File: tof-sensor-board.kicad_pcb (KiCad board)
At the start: 2 copper layers, 22.8 x 16.8 mm, 30 parts, among them U1 STM32F302K8U6, U2 LTC2875, U3 MCP1703, U4 VL53L0X, X1 16MHz

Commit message: routing finished
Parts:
- added G***: LOGO, _logo:CVRA-logo-small, B.Cu at (59.0, 56.0)
- C7: moved to F.Cu
- moved R8 4.10 mm to (49.7, 57.0), turned to 180 degrees
- moved C11 2.64 mm to (55.6, 56.4), turned to 270 degrees
- moved C7 2.61 mm to (53.4, 53.7), turned to 180 degrees
- moved R9 1.12 mm to (47.7, 52.6), turned to 0 degrees
- moved C1 0.58 mm to (53.7, 53.3)
- moved C14 0.22 mm to (52.9, 48.0)
- moved C13 0.20 mm to (46.7, 48.2), turned to 270 degrees
- moved C2 0.20 mm to (47.7, 48.2), turned to 270 degrees
- moved U2 0.20 mm to (53.1, 56.0)
- moved R6 0.14 mm to (49.5, 54.1)
- moved R7 0.14 mm to (50.5, 54.1), turned to 90 degrees
- moved D2 0.10 mm to (49.3, 54.3)
- moved D3 0.10 mm to (50.7, 54.3)
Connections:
- MEC1 pad 1: (no net) -> GND
- MEC2 pad 1: (no net) -> GND
- U1 pad 10: (no net) -> /Proximity
- U1 pad 11: /Proximity -> /Error
- U1 pad 12: /Error -> (no net)
- U1 pad 33: (no net) -> GND
- U2 pad 9: Net-(U2-Pad9) -> GND
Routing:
- net GND: track 28.1 -> 80.9 mm, vias 1 -> 8
- net /CAN_SPEED: track 1.57 -> 5.77 mm
- net Net-(R8-Pad1): track 6.10 -> 2.00 mm
- net Net-(CONN2-Pad4): track 26.1 -> 23.1 mm
- net Net-(D3-Pad2): track 3.66 -> 1.20 mm
- net VCC: track 42.7 -> 44.5 mm
- net Net-(CONN2-Pad3): track 29.2 -> 27.5 mm
- net Net-(U2-Pad9): track 1.61 -> 0.00 mm
- net /CAN_TX: track 9.60 -> 11.0 mm
- net +5V: track 28.3 -> 26.9 mm
- net /GPIO1: track 2.81 -> 3.81 mm
- net /XSHUT: track 1.56 -> 2.44 mm
- net /Proximity: track 1.84 -> 1.28 mm
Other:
- rule trace_min: 0.1524 -> 0.16
- board text added: "CVRA"
- board text added: "VL53L0X TOF Sensor RevA"

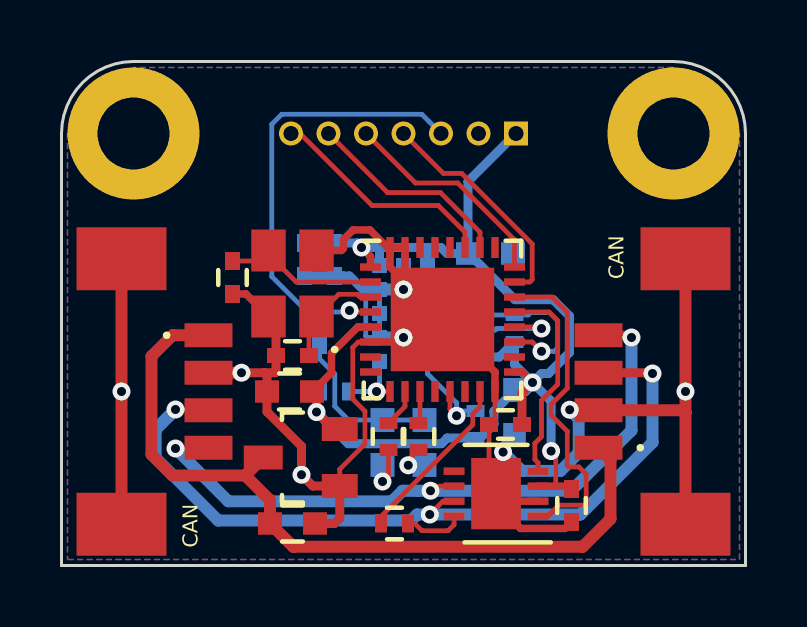
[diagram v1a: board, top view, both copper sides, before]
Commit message: set solder stop mask and solder paste clearance
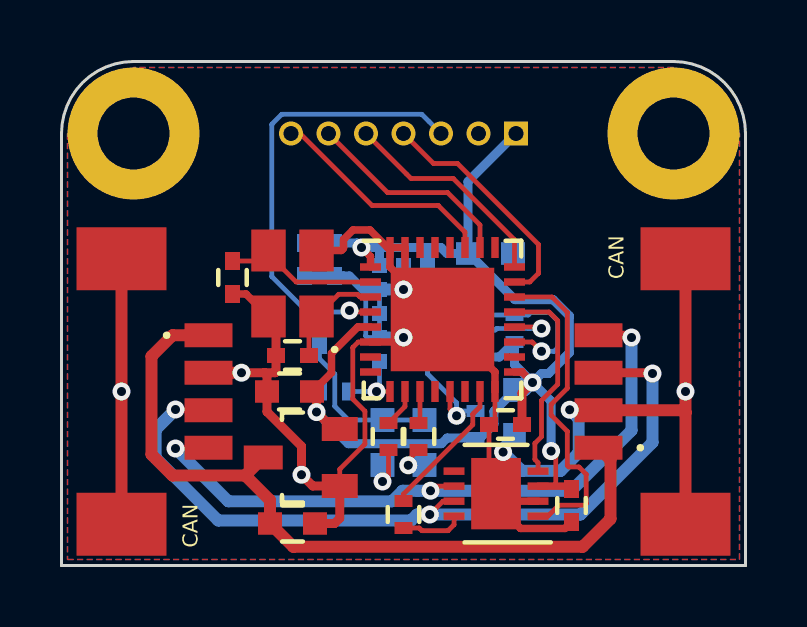
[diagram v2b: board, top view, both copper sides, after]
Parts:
- moved R8 0.42 mm to (50.0, 56.7), turned to 90 degrees
- moved G*** 0.36 mm to (59.2, 56.3)
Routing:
- net /CAN_SPEED: track 5.77 -> 4.71 mm
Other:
- rule pad_to_mask_clearance: 0 -> 0.1
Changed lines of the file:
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@@
 (kicad_pcb (version 4) (host pcbnew 4.0.1-stable)
   (general
-    (links 0)
+    (links 93)
     (no_connects 0)
     (area 38.549999 41.549999 61.450001 58.450001)
-    (thickness 1.6)
+    (thickness 1)
     (drawings 12)
-    (tracks 348)
+    (tracks 349)
     (zones 0)
     (modules 31)
@@
     (pad_size 0.83 1.19)
     (pad_drill 0)
-    (pad_to_mask_clearance 0)
+    (pad_to_mask_clearance 0.1)
+    (solder_mask_min_width 0.1)
+    (pad_to_paste_clearance_ratio -0.05)
     (aux_axis_origin 38.6 58.4)
     (grid_origin 49.2 58.3)
@@
   )
   (module Resistors_SMD:R_0402 (layer F.Cu)
-    (at 49.7 57 180)
+    (at 50 56.7 90)
     (descr "Resistor SMD 0402, reflow soldering, Vishay (see dcrcw.pdf)")
     (tags "resistor 0402")
     (attr smd)
-    (fp_text reference R8 (at 0 -1.8 180) (layer F.SilkS) hide
-      (effects (font (size 1 1) (thickness 0.15)))
-    )
-    (fp_text value 1k (at 0 1.8 180) (layer F.Fab) hide
+    (fp_text reference R8 (at 0 -1.8 90) (layer F.SilkS) hide
+      (effects (font (size 1 1) (thickness 0.15)))
+    )
+    (fp_text value 1k (at 0 1.8 90) (layer F.Fab) hide
       (effects (font (size 1 1) (thickness 0.15)))
     )
@@
     (fp_line (start 0.25 -0.525) (end -0.25 -0.525) (layer F.SilkS) (width 0.15))
     (fp_line (start -0.25 0.525) (end 0.25 0.525) (layer F.SilkS) (width 0.15))
-    (pad 1 smd rect (at -0.45 0 180) (size 0.4 0.6) (layers F.Cu F.Paste F.Mask)
+    (pad 1 smd rect (at -0.45 0 90) (size 0.4 0.6) (layers F.Cu F.Paste F.Mask)
       (net 20 "Net-(R8-Pad1)"))
-    (pad 2 smd rect (at 0.45 0 180) (size 0.4 0.6) (layers F.Cu F.Paste F.Mask)
+    (pad 2 smd rect (at 0.45 0 90) (size 0.4 0.6) (layers F.Cu F.Paste F.Mask)
       (net 21 /CAN_SPEED))
     (model Resistors_SMD.3dshapes/R_0402.wrl
@@
   )
   (module _logo:CVRA-logo-small (layer B.Cu)
-    (at 59 56 90)
+    (at 59.2 56.3 90)
     (fp_text reference G*** (at 0 0 90) (layer B.SilkS) hide
       (effects (font (thickness 0.3)) (justify mirror))
@@
     (effects (font (size 1.2 1.2) (thickness 0.2)) (justify left mirror))
   )
-  (gr_text CVRA (at 59 50.2 270) (layer B.SilkS)
+  (gr_text CVRA (at 59.2 50.6 270) (layer B.SilkS)
     (effects (font (size 2 2) (thickness 0.4)) (justify mirror))
   )
@@
   (segment (start 46.425 48.95) (end 45.5 48.025) (width 0.16) (layer F.Cu) (net 6))
   (segment (start 45.5 48.025) (end 45.5 47.9) (width 0.16) (layer F.Cu) (net 6))
-  (segment (start 50 44) (end 51.32999 45.32999) (width 0.16) (layer F.Cu) (net 7))
-  (segment (start 51.32999 45.32999) (end 51.939554 45.32999) (width 0.16) (layer F.Cu) (net 7))
-  (segment (start 54.290001 48.869999) (end 54.21 48.95) (width 0.16) (layer F.Cu) (net 7))
-  (segment (start 51.939554 45.32999) (end 54.290001 47.680437) (width 0.16) (layer F.Cu) (net 7))
-  (segment (start 54.21 48.95) (end 53.7 48.95) (width 0.16) (layer F.Cu) (net 7))
-  (segment (start 54.290001 47.680437) (end 54.290001 48.869999) (width 0.16) (layer F.Cu) (net 7))
-  (segment (start 48.75 44) (end 50.4 45.65) (width 0.16) (layer F.Cu) (net 8))
-  (segment (start 50.4 45.65) (end 51.807002 45.65) (width 0.16) (layer F.Cu) (net 8))
-  (segment (start 51.807002 45.65) (end 53.7 47.542998) (width 0.16) (layer F.Cu) (net 8))
-  (segment (start 53.7 47.542998) (end 53.7 48.45) (width 0.16) (layer F.Cu) (net 8))
-  (segment (start 47.5 44) (end 49.47001 45.97001) (width 0.16) (layer F.Cu) (net 9))
-  (segment (start 49.47001 45.97001) (end 51.23001 45.97001) (width 0.16) (layer F.Cu) (net 9))
-  (segment (start 51.23001 45.97001) (end 52.55 47.29) (width 0.16) (layer F.Cu) (net 9))
-  (segment (start 52.55 47.29) (end 52.55 47.8) (width 0.16) (layer F.Cu) (net 9))
+  (segment (start 53.7 48.95) (end 54.21 48.95) (width 0.16) (layer F.Cu) (net 7))
+  (segment (start 54.21 48.95) (end 54.5 48.66) (width 0.16) (layer F.Cu) (net 7))
+  (segment (start 54.5 48.66) (end 54.5 47.7) (width 0.16) (layer F.Cu) (net 7))
+  (segment (start 54.5 47.7) (end 51.8 45) (width 0.16) (layer F.Cu) (net 7))
+  (segment (start 51 45) (end 50 44) (width 0.16) (layer F.Cu) (net 7))
+  (segment (start 51.8 45) (end 51 45) (width 0.16) (layer F.Cu) (net 7))
+  (segment (start 53.7 48.45) (end 53.7 47.542998) (width 0.16) (layer F.Cu) (net 8))
+  (segment (start 53.7 47.542998) (end 51.657002 45.5) (width 0.16) (layer F.Cu) (net 8))
+  (segment (start 50.25 45.5) (end 50.1 45.35) (width 0.16) (layer F.Cu) (net 8))
+  (segment (start 51.657002 45.5) (end 50.25 45.5) (width 0.16) (layer F.Cu) (net 8))
+  (segment (start 50.1 45.35) (end 48.75 44) (width 0.16) (layer F.Cu) (net 8))
+  (segment (start 52.55 47.8) (end 52.55 47.05) (width 0.16) (layer F.Cu) (net 9))
+  (segment (start 52.55 47.05) (end 51.47001 45.97001) (width 0.16) (layer F.Cu) (net 9))
+  (segment (start 51.47001 45.97001) (end 49.47001 45.97001) (width 0.16) (layer F.Cu) (net 9))
+  (segment (start 49.47001 45.97001) (end 47.5 44) (width 0.16) (layer F.Cu) (net 9))
   (segment (start 46.25 44) (end 46.552798 44) (width 0.16) (layer F.Cu) (net 10))
   (segment (start 46.552798 44) (end 48.952798 46.4) (width 0.16) (layer F.Cu) (net 10))
@@
   (segment (start 50.55 52.6) (end 50.55 53.6) (width 0.16) (layer F.Cu) (net 19))
   (segment (start 50.55 53.6) (end 50.5 53.65) (width 0.16) (layer F.Cu) (net 19))
-  (segment (start 50.15 57) (end 50.375796 57) (width 0.16) (layer F.Cu) (net 20))
-  (segment (start 50.375796 57) (end 50.615797 57.240001) (width 0.16) (layer F.Cu) (net 20))
+  (segment (start 50 57.15) (end 50.525796 57.15) (width 0.16) (layer F.Cu) (net 20))
+  (segment (start 50.525796 57.15) (end 50.615797 57.240001) (width 0.16) (layer F.Cu) (net 20))
   (segment (start 50.615797 57.240001) (end 51.484999 57.240001) (width 0.16) (layer F.Cu) (net 20))
   (segment (start 51.484999 57.240001) (end 51.685 57.04) (width 0.16) (layer F.Cu) (net 20))
   (segment (start 51.685 57.04) (end 51.685 56.755) (width 0.16) (layer F.Cu) (net 20))
-  (segment (start 49.25 57) (end 49.25 56.767516) (width 0.16) (layer F.Cu) (net 21))
-  (segment (start 52.309999 53.350001) (end 52.55 53.11) (width 0.16) (layer F.Cu) (net 21))
-  (segment (start 49.25 56.767516) (end 52.309999 53.707517) (width 0.16) (layer F.Cu) (net 21))
-  (segment (start 52.309999 53.707517) (end 52.309999 53.350001) (width 0.16) (layer F.Cu) (net 21))
+  (segment (start 50 56.25) (end 50 56.017516) (width 0.16) (layer F.Cu) (net 21))
+  (segment (start 52.30999 53.707526) (end 52.30999 53.35001) (width 0.16) (layer F.Cu) (net 21))
+  (segment (start 50 56.017516) (end 52.30999 53.707526) (width 0.16) (layer F.Cu) (net 21))
+  (segment (start 52.30999 53.35001) (end 52.55 53.11) (width 0.16) (layer F.Cu) (net 21))
   (segment (start 52.55 53.11) (end 52.55 52.6) (width 0.16) (layer F.Cu) (net 21))
   (segment (start 48.15 52.6) (end 49.1 52.6) (width 0.16) (layer B.Cu) (net 22))
